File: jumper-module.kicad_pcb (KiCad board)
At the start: 2 copper layers, 16.3 x 21.3 mm, 11 parts, among them J1 , J10 Conn_01x08, J101 Conn_01x08, J9 Conn_01x08, J91 Conn_01x08

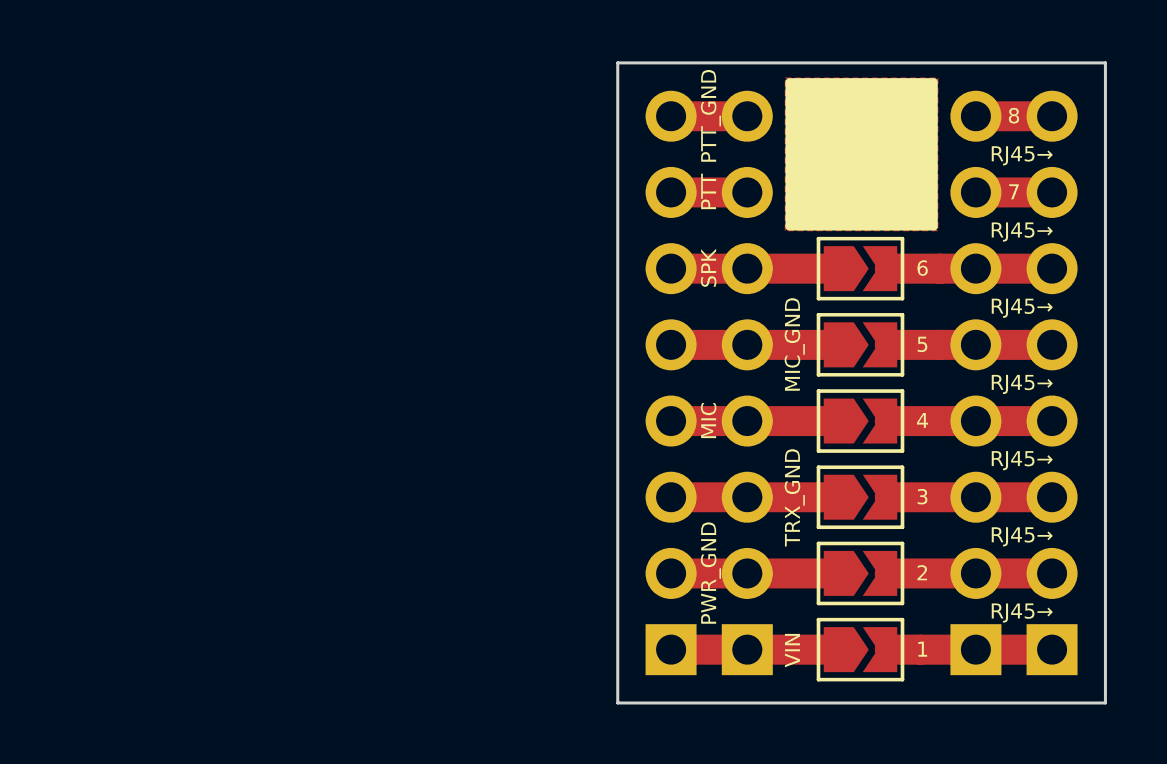
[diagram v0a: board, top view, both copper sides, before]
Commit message: Added bottom silkscreen and changed board size
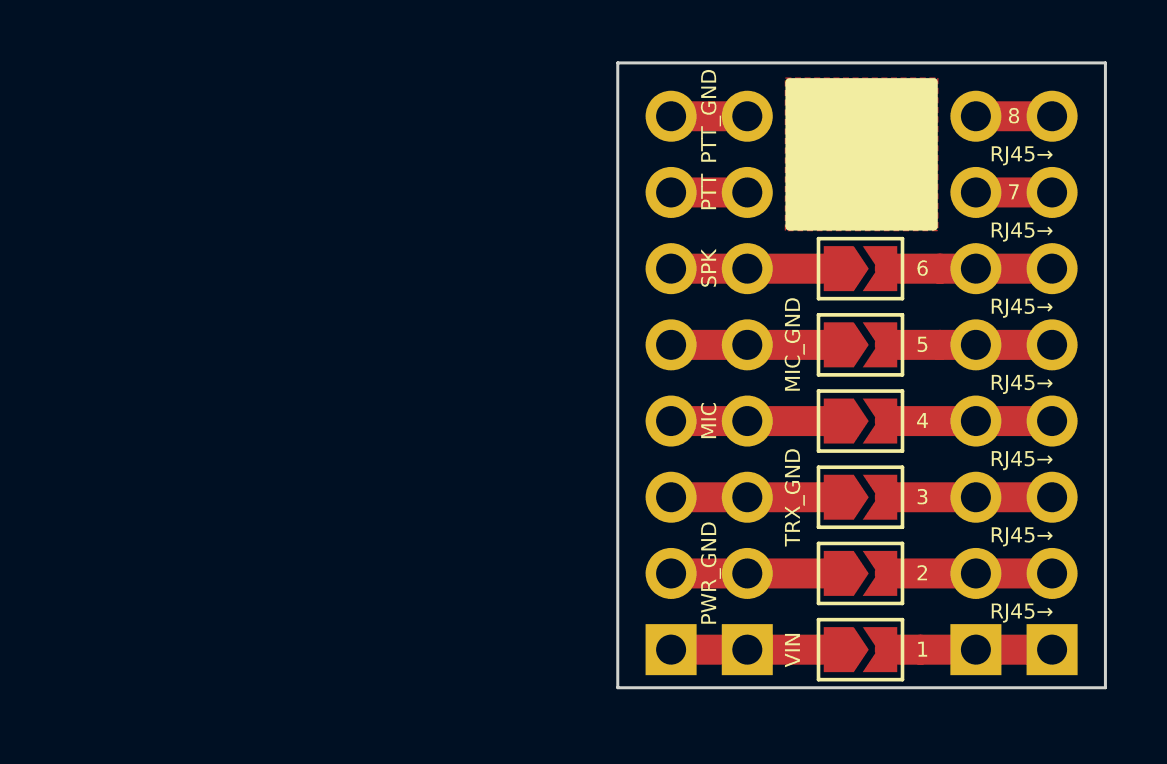
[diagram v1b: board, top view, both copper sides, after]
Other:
- board size 16.3 x 21.3 mm -> 16.3 x 20.8 mm
- board text added: "bt-trx.com Generic Jumper Module"
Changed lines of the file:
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@@
   (general
     (thickness 1.6)
-    (drawings 27)
+    (drawings 28)
     (tracks 31)
     (zones 0)
@@
   )
   (page A4)
+  (title_block
+    (title "Generic Jumper Module")
+    (date 2020-01-22)
+    (rev v1)
+    (company bt-trx.com)
+    (comment 1 "Licensed under CERN OHL v1.2 - https://ohwr.org/licenses/cern-ohl/v1.2")
+    (comment 2 "Andreas Müller - DC1MIL")
+    (comment 3 "Christian Obersteiner - DL1COM")
+    (comment 4 Authors:)
+  )
   (layers
     (0 F.Cu signal)
@@
       ))
   )
+  (gr_text "bt-trx.com\nGeneric Jumper Module" (at 141.478 98.806 270) (layer B.SilkS)
+    (effects (font (size 1 0.8) (thickness 0.15)) (justify mirror))
+  )
   (gr_text PWR_GND (at 136.398 102.87 90) (layer F.SilkS)
     (effects (font (size 0.5 0.5) (thickness 0.125)))
@@
     (effects (font (size 0.5 0.5) (thickness 0.125)))
   )
-  (gr_line (start 149.606 85.852) (end 149.606 107.188) (layer Edge.Cuts) (width 0.1))
+  (gr_line (start 149.606 85.852) (end 149.606 106.68) (layer Edge.Cuts) (width 0.1))
   (gr_line (start 133.35 85.852) (end 149.606 85.852) (layer Edge.Cuts) (width 0.1))
-  (gr_line (start 133.35 107.188) (end 133.35 85.852) (layer Edge.Cuts) (width 0.1))
-  (gr_line (start 149.606 107.188) (end 133.35 107.188) (layer Edge.Cuts) (width 0.1))
+  (gr_line (start 133.35 106.68) (end 133.35 85.852) (layer Edge.Cuts) (width 0.1))
+  (gr_line (start 149.606 106.68) (end 133.35 106.68) (layer Edge.Cuts) (width 0.1))
   (segment (start 135.128 87.63) (end 137.668 87.63) (width 1) (layer F.Cu) (net 2))
   (segment (start 135.128 90.17) (end 137.668 90.17) (width 1) (layer F.Cu) (net 3))

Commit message: Non generic Handheld JM
Created first verion of non generic handheld jumper module
for kenwood handhelds
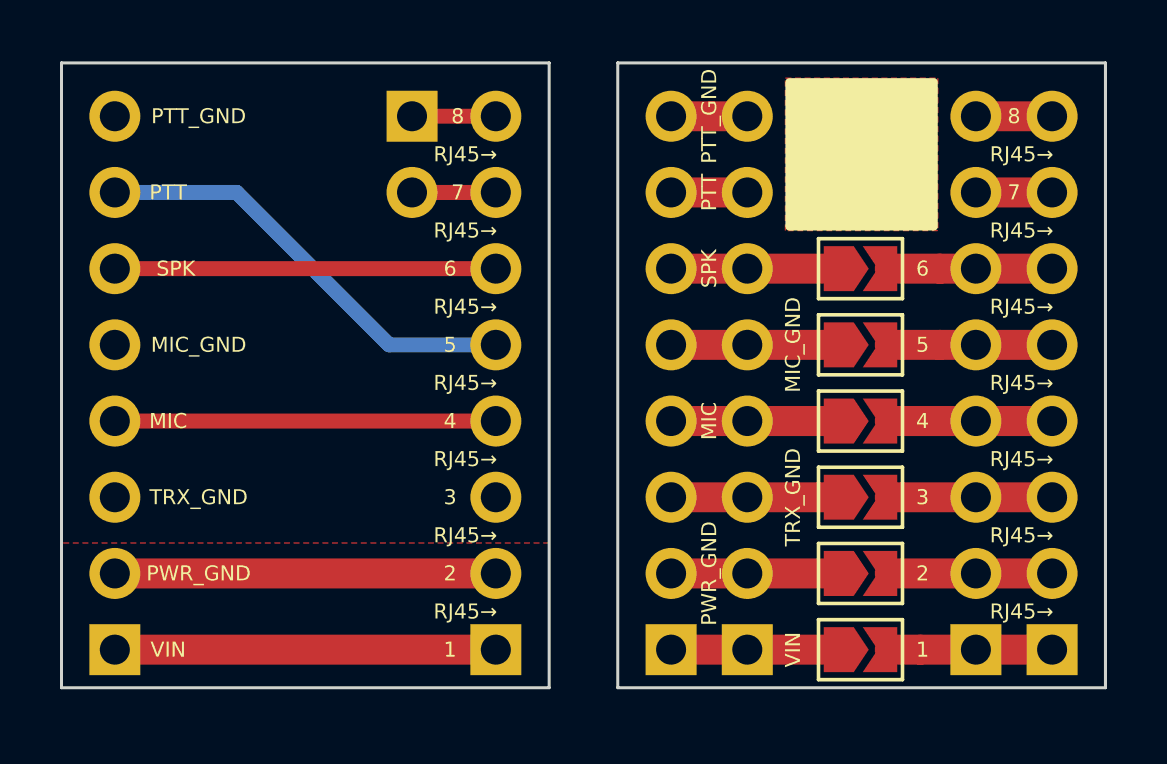
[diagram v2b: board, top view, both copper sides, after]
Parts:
- added JKH10: Conn_01x08, Connector_PinHeader_2.54mm:PinHeader_1x08_P2.54mm_Vertical, F.Cu at (129.3, 105.4)
- added JKH101: Conn_01x02, Connector_PinHeader_2.54mm:PinHeader_1x02_P2.54mm_Vertical, F.Cu at (126.5, 87.6)
- added JKH9: Conn_01x08, Connector_PinHeader_2.54mm:PinHeader_1x08_P2.54mm_Vertical, F.Cu at (116.6, 105.4)
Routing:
- net /PTT_KH: track 0.00 -> 14.8 mm
- net /V_IN_KH: track 0.00 -> 12.7 mm
- net /SPK_KH: track 0.00 -> 12.7 mm
- net /PWR_GND_KH: track 0.00 -> 12.7 mm
- net /MIC_KH: track 0.00 -> 12.7 mm
- net Net-(JKH10-Pad8): track 0.00 -> 2.79 mm
- net Net-(JKH10-Pad7): track 0.00 -> 2.79 mm
- added copper zone on F.Cu, net /TRX_GND_KH
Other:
- board size 16.3 x 20.8 mm -> 34.8 x 20.8 mm
- board text added: "bt-trx.com Kenwood Handheld"
